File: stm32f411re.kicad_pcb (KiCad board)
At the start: 2 copper layers, 32 parts, among them J1 ADC, J2 USB_OTG, J3 SD, J4 SPI, J5 UART, J6 I2C, J7 GPIO_Digital_I/O, J8 GPIO_Analog_pins, SW1 BOOT_SW, SW2 SW_Push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

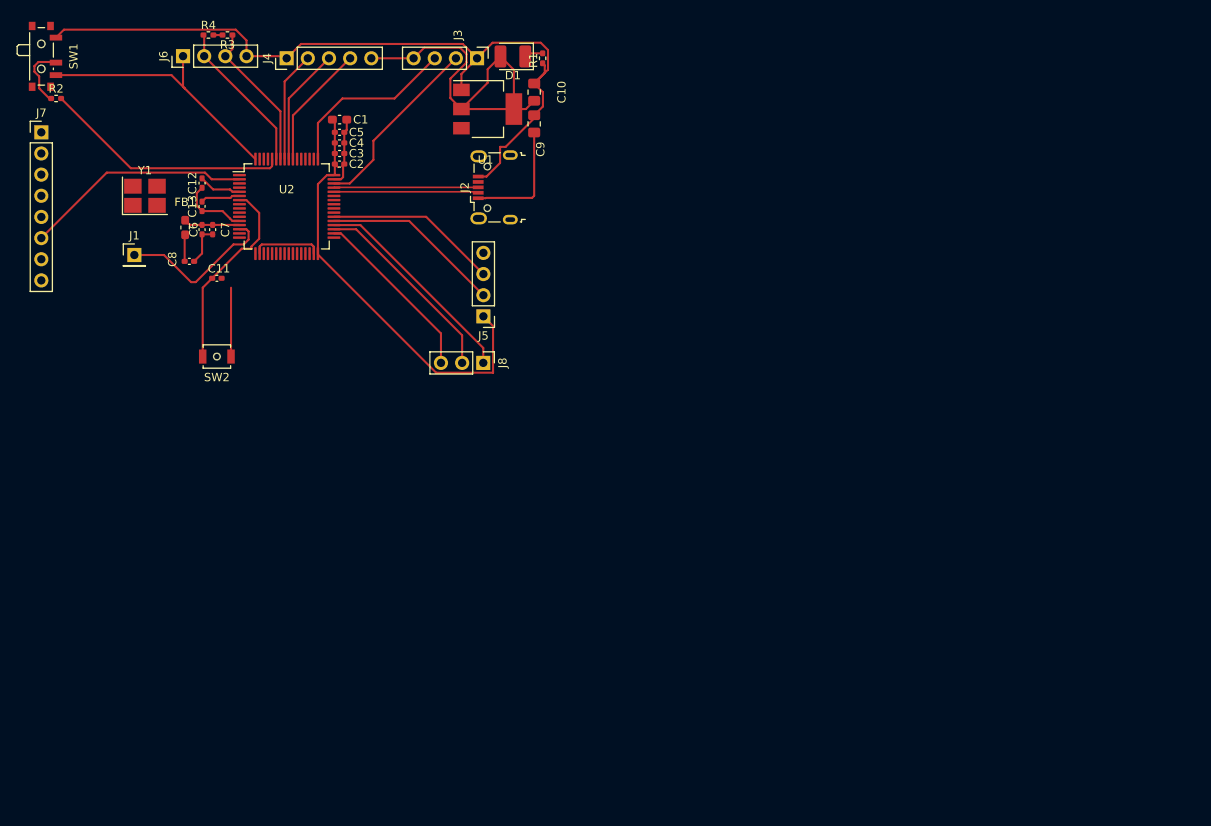
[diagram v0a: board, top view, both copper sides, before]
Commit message: removed the GPIO input and outpins (want to redo them) and mostly finished the first pcb layout
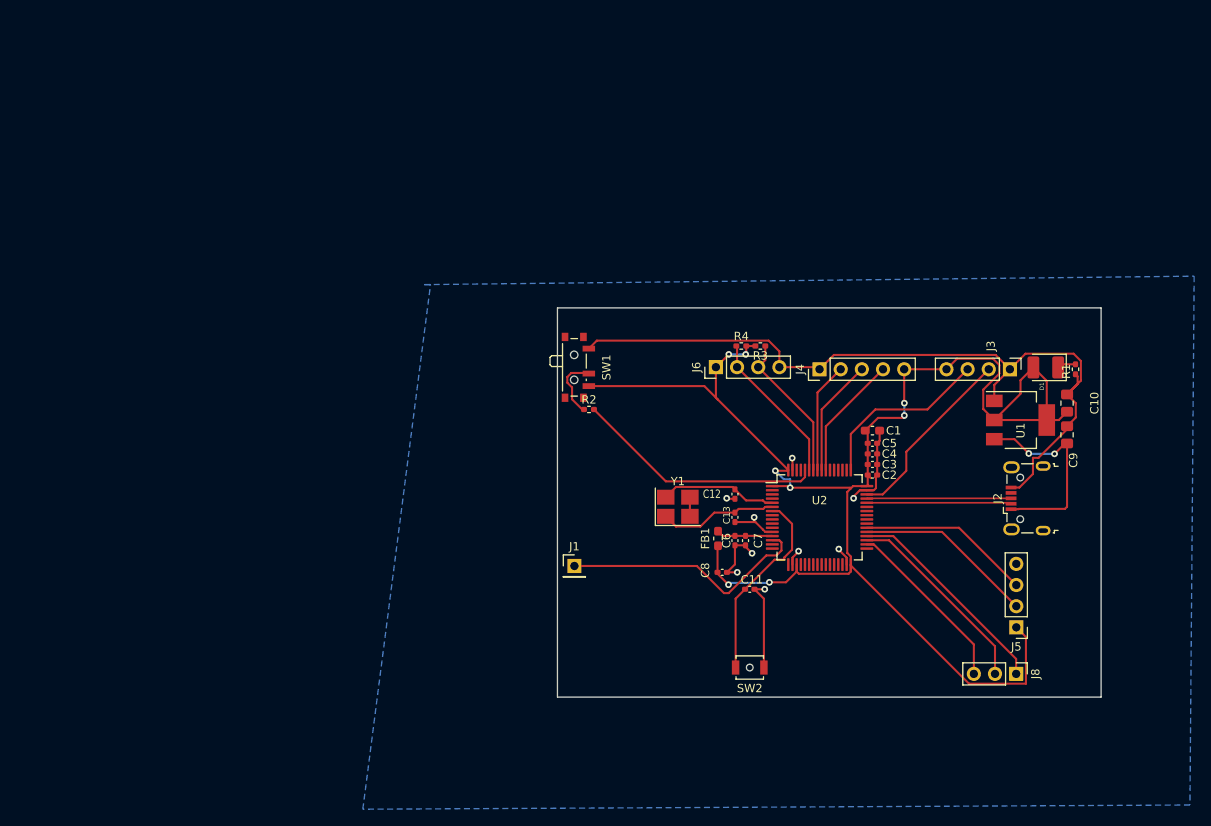
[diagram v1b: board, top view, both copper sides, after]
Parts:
- removed J7: GPIO_Digital_I/O, Connector_PinHeader_2.54mm:PinHeader_1x08_P2.54mm_Vertical
- moved C2 74.1 mm to (159.2, 105.9)
- moved C5 74.1 mm to (159.2, 102.1)
- moved C1 74.1 mm to (159.2, 100.6)
- moved C10 74.1 mm to (182.6, 97.3)
- moved C13 74.1 mm to (142.7, 111.0)
- moved C3 74.1 mm to (159.2, 104.7)
- moved C4 74.1 mm to (159.2, 103.4)
- moved C6 74.1 mm to (142.7, 113.8)
- moved C7 74.1 mm to (144.0, 113.8)
- moved C8 74.1 mm to (141.2, 117.6)
- moved C9 74.1 mm to (182.6, 101.1)
- moved FB1 74.1 mm to (140.7, 113.5)
- moved J3 74.1 mm to (175.7, 93.2)
- moved J5 74.1 mm to (176.5, 124.2)
- moved J6 74.1 mm to (140.4, 93.0)
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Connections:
- U2 pad 2: /GPIO_OUT(PC13) -> unconnected-(U2-PC13-Pad2)
- U2 pad 3: /GPIO_OUT(PC14) -> unconnected-(U2-PC14-Pad3)
- U2 pad 39: /GPIO_IN(PC8) -> unconnected-(U2-PC8-Pad39)
- U2 pad 4: /GPIO_OUT(PC15) -> unconnected-(U2-PC15-Pad4)
- U2 pad 40: /GPIO_IN(PC9) -> unconnected-(U2-PC9-Pad40)
- U2 pad 51: /GPIO_IN(PC10) -> unconnected-(U2-PC10-Pad51)
- U2 pad 52: /GPIO_IN(PC11) -> unconnected-(U2-PC11-Pad52)
- U2 pad 53: /GPIO_OUT(PC12) -> unconnected-(U2-PC12-Pad53)
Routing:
- net +3.3V: track 133.8 -> 184.7 mm, vias 0 -> 8
- net /GPIO_OUT(PC13): track 27.4 -> 0.00 mm
- net /ADC: track 19.4 -> 30.5 mm
- net VBUS: track 14.4 -> 24.4 mm, vias 0 -> 2
- net /HSE_OUT: track 4.77 -> 14.3 mm
- net /HSE_IN: track 5.15 -> 14.1 mm
- net GND: track 131.5 -> 134.5 mm, vias 0 -> 9
- net Net-(Y1-Pad2): track 0.00 -> 2.30 mm
- added copper zone on B.Cu, net GND
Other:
- board outline added: 65.3 x 46.7 mm

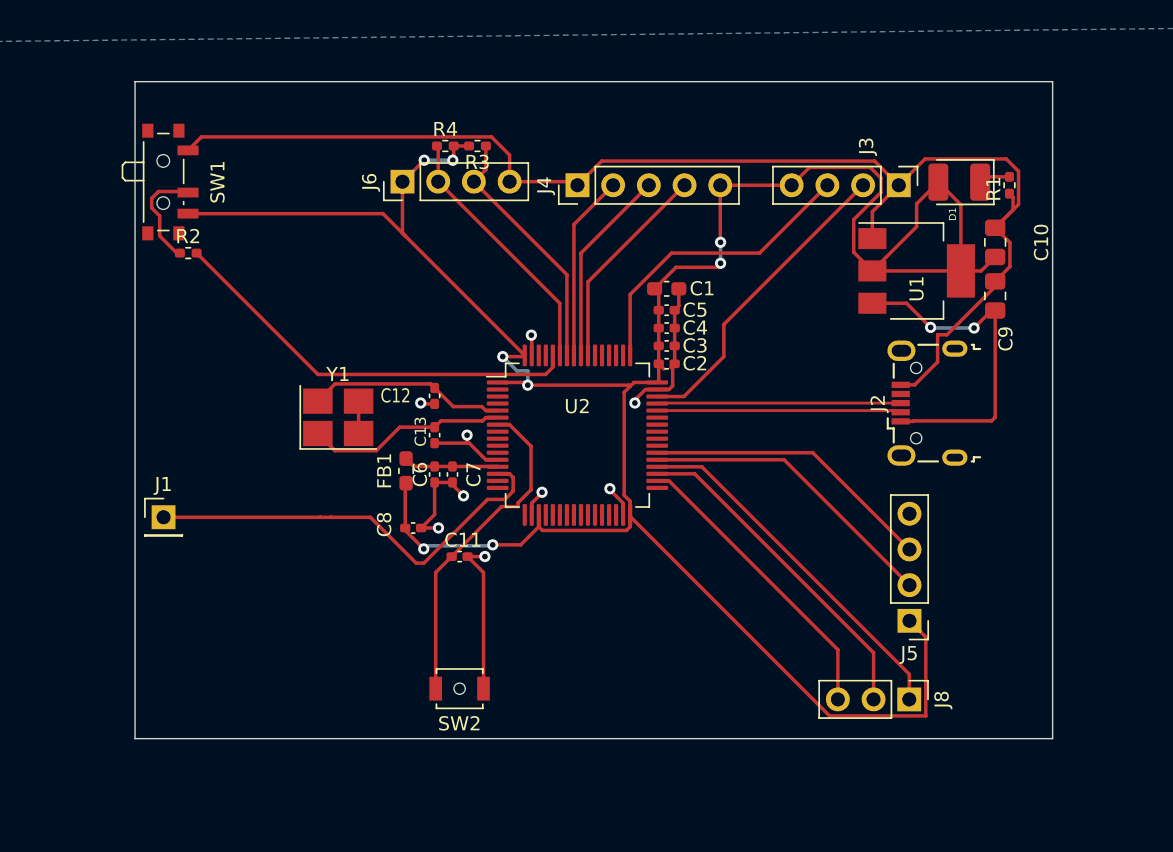
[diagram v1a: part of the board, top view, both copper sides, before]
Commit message: PCB changes
changed form factor, finished PCB, and ran DRC

:wq
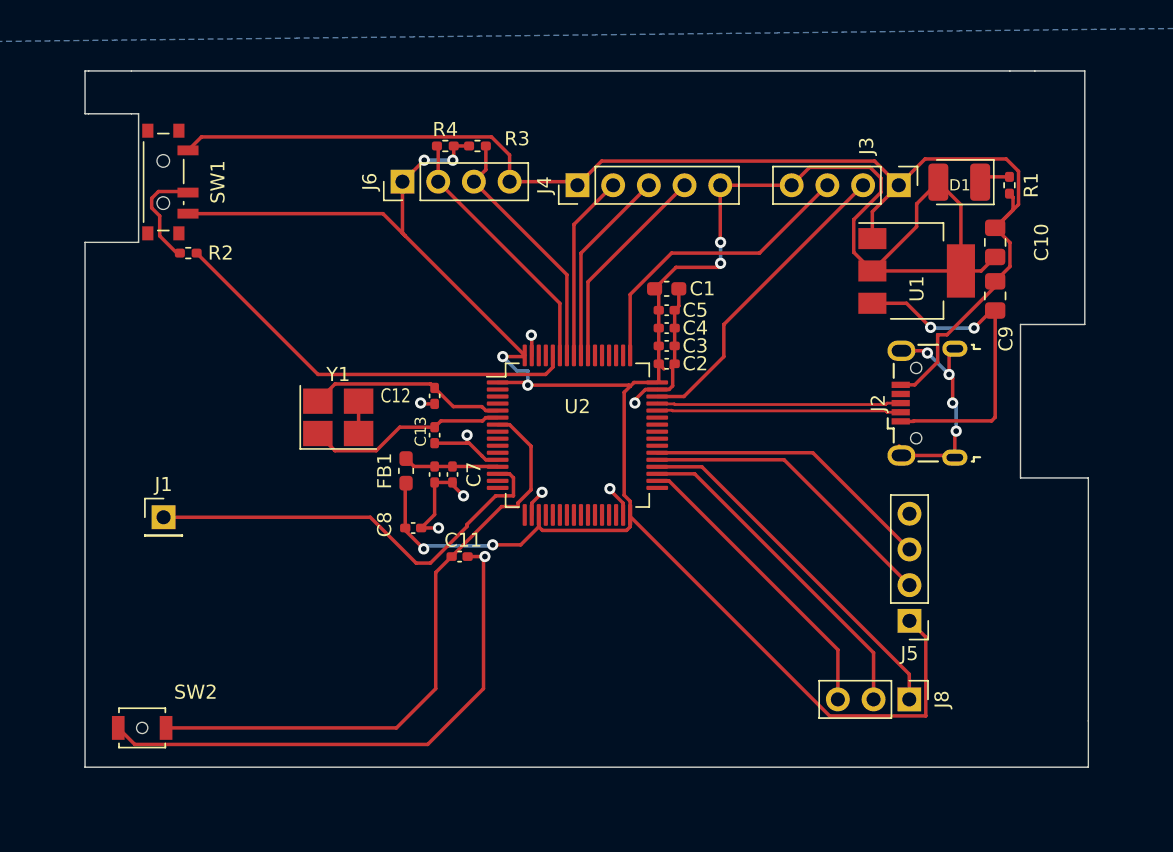
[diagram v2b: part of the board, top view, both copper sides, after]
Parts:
- moved SW2 22.8 mm to (121.9, 131.8), turned to 0 degrees
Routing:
- net GND: track 134.5 -> 162.1 mm
- net /NRST: track 23.8 -> 44.1 mm
- net unconnected-(J2-Shield-Pad6): track 0.21 -> 16.9 mm, vias 0 -> 4
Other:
- board size 65.3 x 46.7 mm -> 71.4 x 49.5 mm
